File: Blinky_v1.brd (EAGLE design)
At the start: 25.4 x 31.8 mm, 11 parts

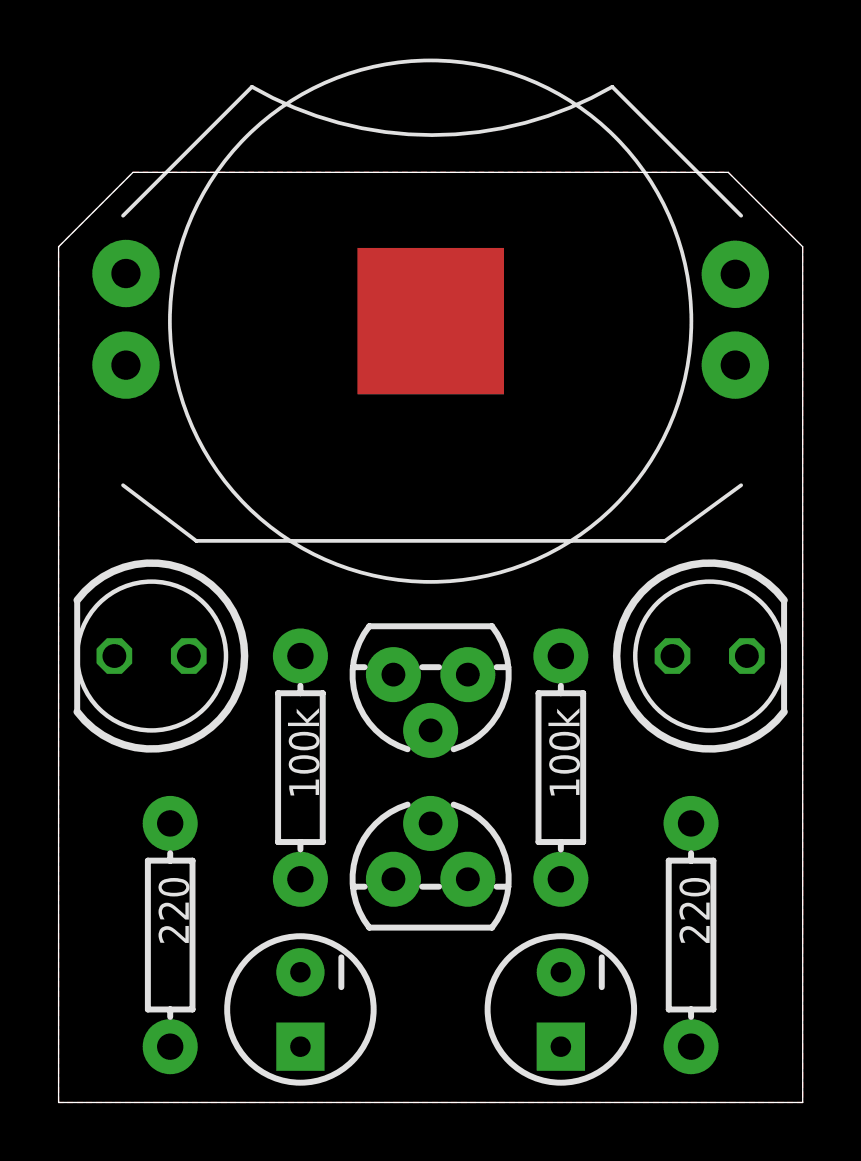
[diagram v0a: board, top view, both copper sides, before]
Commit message: Added good and bad soldering image, top and bottom text. All on bottom silkscreen.
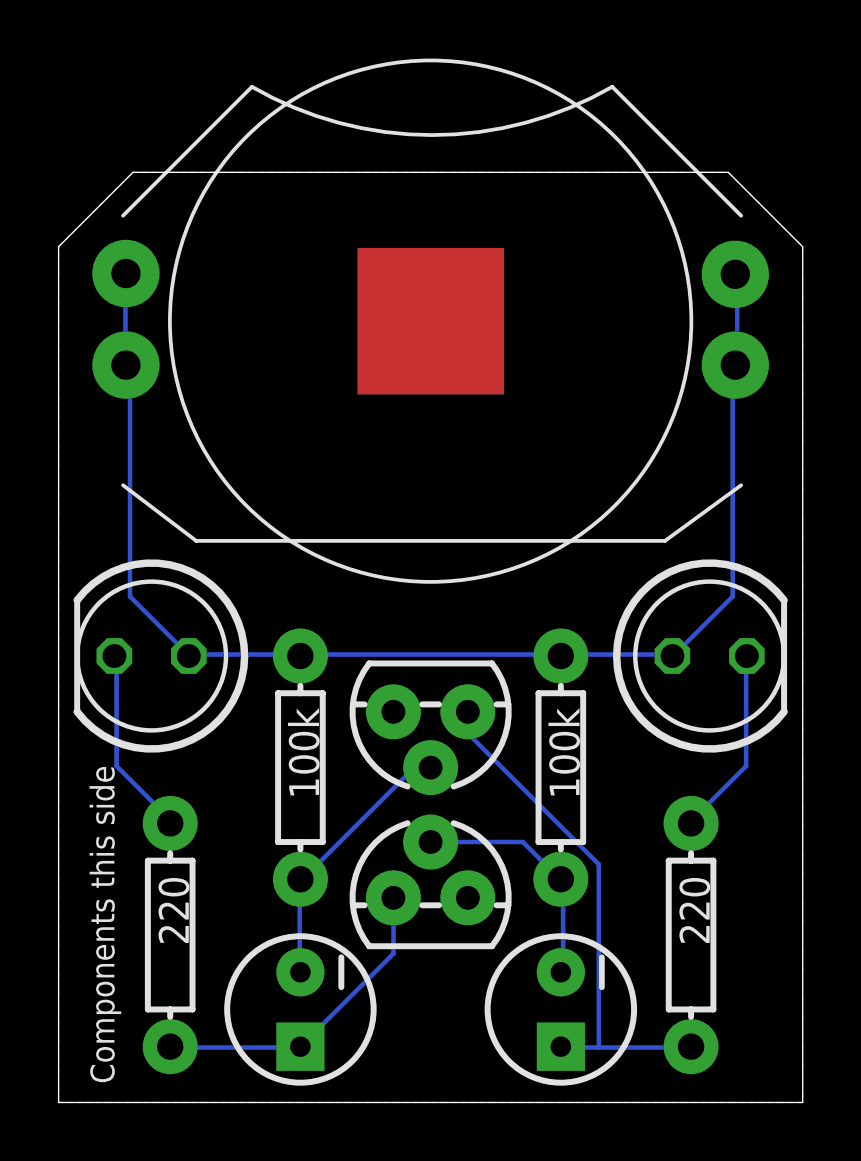
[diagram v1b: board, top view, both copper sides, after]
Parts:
- moved U$2 1.27 mm to (12.7, 19.7)
- moved U$1 0.63 mm to (12.7, 13.3)
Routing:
- net N$5: track 0.00 -> 44.6 mm
- net N$2: track 0.00 -> 17.8 mm
- net N$4: track 0.00 -> 10.9 mm
- net N$6: track 0.00 -> 9.22 mm
- net N$7: track 0.00 -> 8.22 mm
- net N$3: track 0.00 -> 6.50 mm
- net N$1: track 0.00 -> 6.49 mm
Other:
- board text added: "Bad"
- board text added: "Collaboration Hack.RVA & Small Hall Makerspace Licensed CC-BY-SA"
- board text added: "Components this side"
- board text added: "Good"
- board text added: "Soldering this side"
- board text removed: "Collaboration Hack.RVA & Small Hall Makerspace Open license CC-BY-SA"
